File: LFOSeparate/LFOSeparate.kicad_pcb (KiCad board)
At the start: 2 copper layers, 100 x 45 mm, 31 parts, among them IC1 PIC16F15325-I_P, IC2 MCP6232-E_P, IC3 MCP6232-E_P, J1 ICSP, J2 D_Power, J3 Input, J4 Output, J5 A_Power, U1 Opamp_Dual

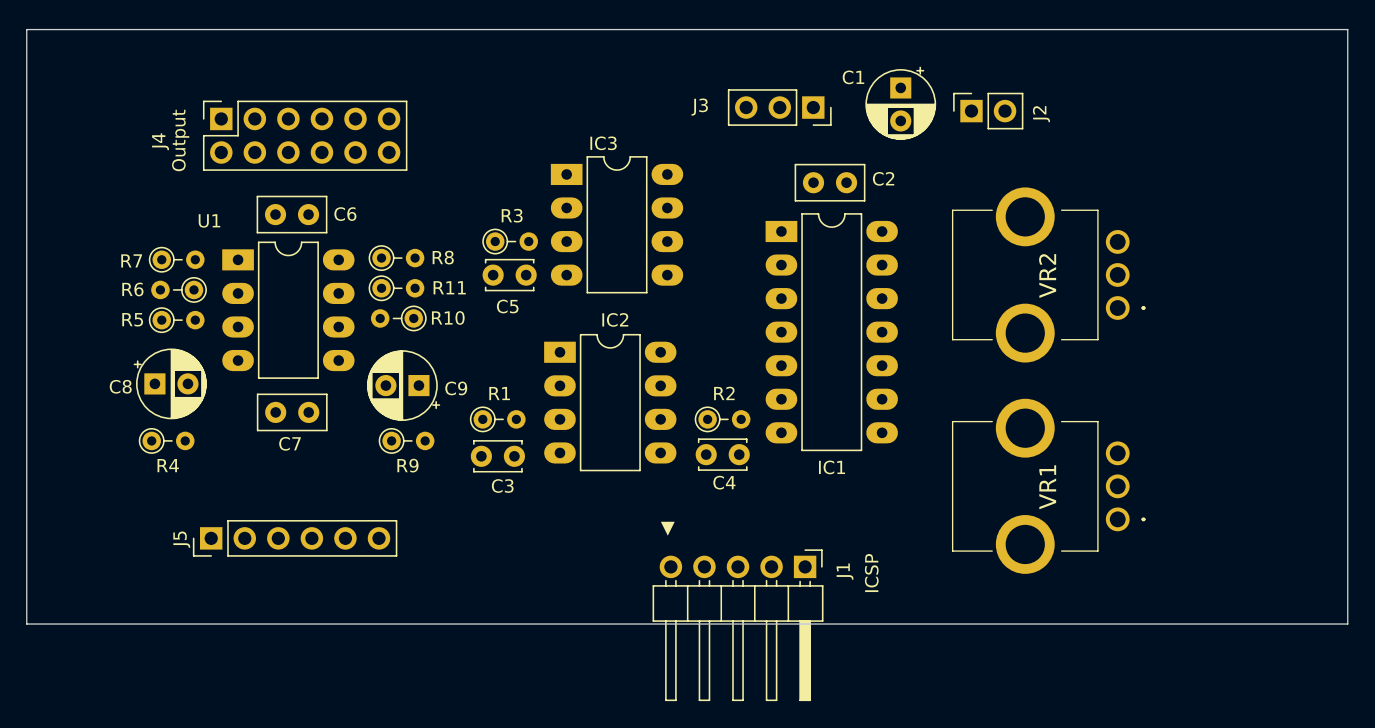
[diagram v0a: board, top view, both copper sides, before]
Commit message: LFOSeparate
LFOSeparateは配線完了
EGSeparateは回路図作成中
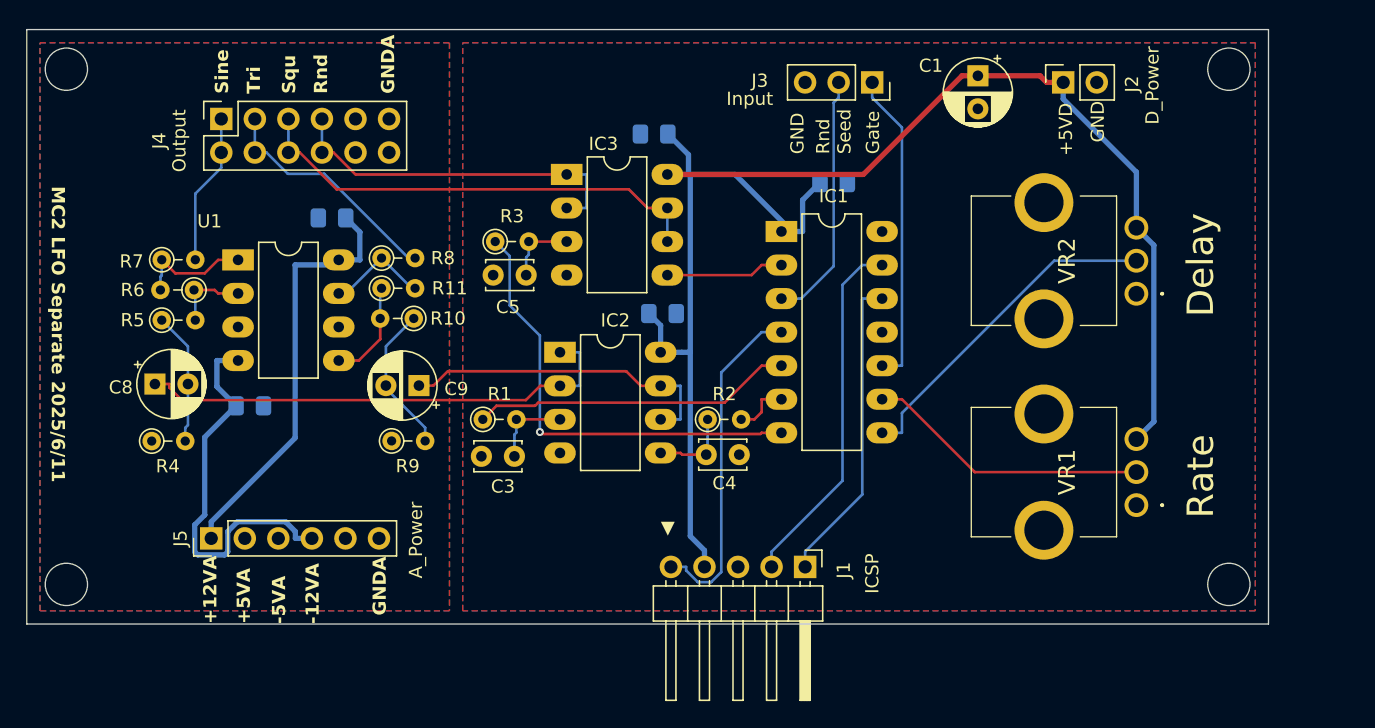
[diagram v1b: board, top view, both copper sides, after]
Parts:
- added C10: 0.1uF, Capacitor_SMD:C_0805_2012Metric_Pad1.18x1.45mm_HandSolder, B.Cu at (134.5, 41.9)
- added C11: 0.1uF, Capacitor_SMD:C_0805_2012Metric_Pad1.18x1.45mm_HandSolder, B.Cu at (135.1, 55.5)
- C2, C6, C7: footprint Capacitor_THT:C_Disc_D5.0mm_W2.5mm_P2.50mm -> Capacitor_SMD:C_0805_2012Metric_Pad1.18x1.45mm_HandSolder; moved to B.Cu
- moved J2 7.28 mm to (165.5, 38.0)
- moved C1 5.91 mm to (159.0, 37.5)
- moved J3 4.85 mm to (151.0, 38.0)
- moved C7 2.02 mm to (103.9, 62.5)
- moved C6 1.80 mm to (110.1, 48.3)
- moved VR1 1.78 mm to (171.0, 70.0)
- moved VR2 1.78 mm to (171.0, 54.0)
- moved C2 1.52 mm to (148.1, 45.6)
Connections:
- VR1 pad 1: +5VD -> GND
- VR1 pad 3: GND -> +5VD
- VR2 pad 1: +5VD -> GND
- VR2 pad 3: GND -> +5VD
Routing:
- net +5VD: track 0.00 -> 120.1 mm
- net Raw_Sine: track 0.00 -> 37.3 mm
- net Square: track 0.00 -> 35.5 mm
- net PWM_Randum: track 0.00 -> 34.2 mm, vias 0 -> 1
- net +12VA: track 0.00 -> 32.0 mm
- net -12VA: track 0.00 -> 29.7 mm
- net Randum: track 0.00 -> 27.3 mm
- net ICSPDT: track 0.00 -> 27.2 mm
- net ~MCLR: track 0.00 -> 25.7 mm
- net Delay: track 0.00 -> 25.5 mm
- net Raw_Triangle: track 0.00 -> 24.7 mm
- net PWM_Sine: track 0.00 -> 24.3 mm
- net Gate: track 0.00 -> 23.9 mm
- net ICSPCLK: track 0.00 -> 23.6 mm
- net Rate: track 0.00 -> 21.5 mm
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- added copper zone on B.Cu, net GND
- added copper zone on F.Cu, net GND
- added copper zone on B.Cu, net GNDA
- added copper zone on F.Cu, net GNDA
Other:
- board size 100 x 45 mm -> 94 x 45 mm
- board text added: "+12VA"
- board text added: "+5VA"
- board text added: "+5VD"
- board text added: "-12VA"
- board text added: "-5VA"
- board text added: "A_Power"
- board text added: "D_Power"
- board text added: "Delay"
- board text added: "GND"
- board text added: "GNDA"
- board text added: "Gate"
- board text added: "Input"
- board text added: "MC2 LFO Separate 2025/6/11"
- board text added: "Rate"
- board text added: "Rnd"
- board text added: "Rnd Seed"
- board text added: "Sine"
- board text added: "Squ"
- board text added: "Tri"

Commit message: MC2
アクセントレベルを追加したEGACCを登録
回路全般部品配置済
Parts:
- added D1: D, Diode_THT:D_DO-34_SOD68_P2.54mm_Vertical_AnodeUp, F.Cu at (94.1, 37.7)
- added D2: LED, LED_THT:LED_D5.0mm_FlatTop, F.Cu at (89.4, 56.6)
- added Q1: Q_NPN_ECB, Package_TO_SOT_THT:TO-92_HandSolder, F.Cu at (91.8, 45.2)
- added R12: 100K, Resistor_THT:R_Axial_DIN0204_L3.6mm_D1.6mm_P2.54mm_Vertical, F.Cu at (94.3, 40.3)
- added R13: 1K, Resistor_THT:R_Axial_DIN0204_L3.6mm_D1.6mm_P2.54mm_Vertical, F.Cu at (92.2, 49.1)
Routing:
- net +12VA: track 32.0 -> 52.3 mm
- net Net-(D2-A): track 0.00 -> 12.0 mm
- net Triangle: track 18.8 -> 27.7 mm
- net Net-(Q1-B): track 0.00 -> 5.97 mm
- net Net-(Q1-C): track 0.00 -> 5.58 mm
- net Net-(D1-K): track 0.00 -> 2.61 mm
- net -12VA: track 29.7 -> 32.1 mm
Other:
- board text added: "MC2 LFO Separate 2025/6/14"
- board text removed: "MC2 LFO Separate 2025/6/11"

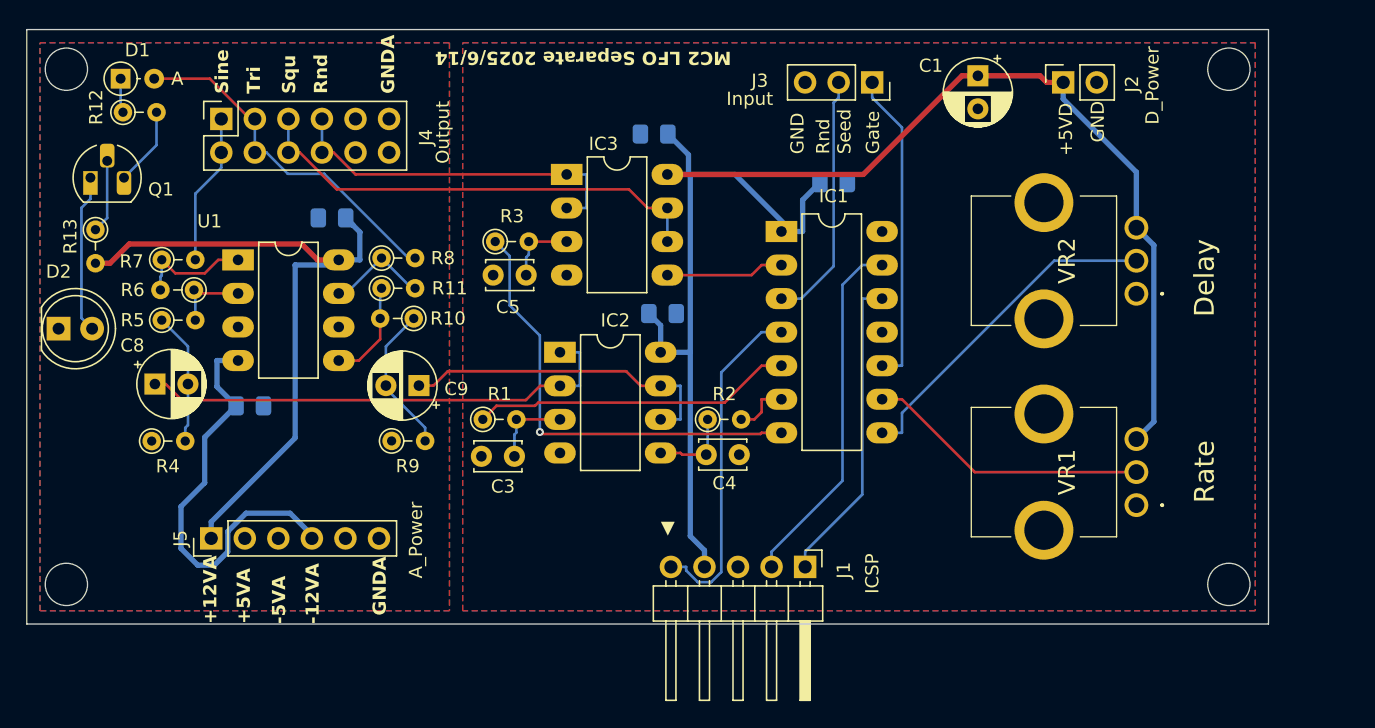
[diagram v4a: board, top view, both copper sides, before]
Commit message: LFOSeparate
プログラムと回路のデバッグ後の修正を反映
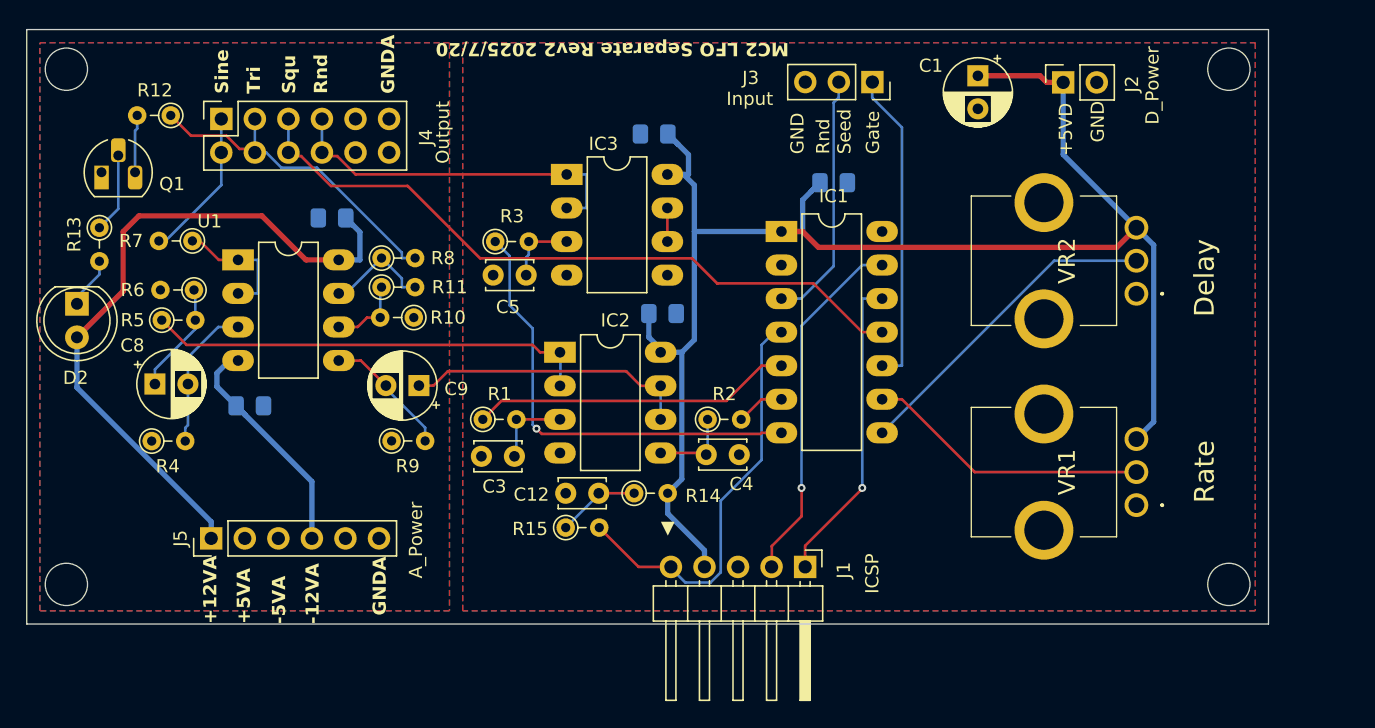
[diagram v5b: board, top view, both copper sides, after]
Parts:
- removed D1: D, Diode_THT:D_DO-34_SOD68_P2.54mm_Vertical_AnodeUp
- added C12: 0.01uF, Capacitor_THT:C_Disc_D3.4mm_W2.1mm_P2.50mm, F.Cu at (130.3, 69.1)
- added R14: 1K, Resistor_THT:R_Axial_DIN0204_L3.6mm_D1.6mm_P2.54mm_Vertical, F.Cu at (133.0, 69.1)
- added R15: 100, Resistor_THT:R_Axial_DIN0204_L3.6mm_D1.6mm_P2.54mm_Vertical, F.Cu at (127.8, 71.7)
- C8, C9: value 1uF/16V -> 47uF/16V
- R11: value 12K -> 1.2K
- R13: value 1K -> 2.2K
- R5: value 10K -> 30K
- R6: value 3.9K -> 20K
- moved R12 3.62 mm to (97.9, 40.5), turned to 180 degrees
- moved R7 2.72 mm to (99.5, 50.0), turned to 180 degrees
- moved D2 2.34 mm to (90.8, 54.8), turned to -90 degrees
- moved Q1 0.93 mm to (92.7, 44.8)
- moved R13 0.33 mm to (92.5, 49.0)
- moved R11 0.08 mm to (113.9, 53.5)
- moved R10 0.07 mm to (116.3, 55.8)
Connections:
- C8 pad 1: Raw_Sine -> Net-(C8-Pad1)
- C8 pad 2: Net-(C8-Pad2) -> Net-(U1A-+)
- C9 pad 2: Net-(C9-Pad2) -> Net-(U1B-+)
- D2 pad 1: GNDA -> Net-(D2-K)
- D2 pad 2: Net-(D2-A) -> +12VA
- IC1 pad 11: unconnected-(IC1-RA2-Pad11) -> Square
- IC1 pad 2: Raw_Square -> unconnected-(IC1-RA5-Pad2)
- IC3 pad 5: Raw_Square -> GND
- IC3 pad 6: Square -> Net-(IC3-VINB-)
- IC3 pad 7: Square -> Net-(IC3-VINB-)
- Q1 pad 1: Net-(D2-A) -> GNDA
- R10 pad 1: Net-(C9-Pad2) -> GNDA
- R10 pad 2: Net-(U1B-+) -> Net-(U1B--)
- R11 pad 1: Net-(U1B-+) -> Net-(U1B--)
- R12 pad 1: Net-(D1-K) -> Triangle
- R13 pad 2: +12VA -> Net-(D2-K)
- R4 pad 2: Net-(C8-Pad2) -> Net-(U1A-+)
- R5 pad 1: Net-(C8-Pad2) -> Raw_Sine
- R5 pad 2: Net-(U1A--) -> Net-(C8-Pad1)
- R6 pad 1: Net-(U1A--) -> Net-(C8-Pad1)
- R6 pad 2: Net-(R6-Pad2) -> GNDA
- R7 pad 1: Net-(R6-Pad2) -> Net-(U1A--)
- R9 pad 2: Net-(C9-Pad2) -> Net-(U1B-+)
- U1 pad 1: Net-(R6-Pad2) -> Net-(U1A--)
- U1 pad 3: GNDA -> Net-(U1A-+)
- U1 pad 6: GNDA -> Net-(U1B--)
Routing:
- net Square: track 35.5 -> 53.1 mm
- net -12VA: track 32.1 -> 18.5 mm
- net Net-(D2-A): track 12.0 -> 0.00 mm
- net Net-(C9-Pad2): track 11.4 -> 0.00 mm
- net Net-(U1A-+): track 0.00 -> 11.2 mm
- net Net-(C8-Pad2): track 10.1 -> 0.00 mm
- net Net-(R6-Pad2): track 8.95 -> 0.00 mm
- net Raw_Square: track 8.95 -> 0.00 mm
- net Net-(C8-Pad1): track 0.00 -> 8.43 mm
- net Net-(C12-Pad1): track 0.00 -> 6.32 mm
- net ~MCLR: track 25.7 -> 31.7 mm
- net Net-(U1B--): track 0.00 -> 5.78 mm
- net Net-(D2-K): track 0.00 -> 3.92 mm
- net Net-(U1A--): track 5.77 -> 9.60 mm
- net Raw_Sine: track 37.2 -> 33.8 mm
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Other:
- board text added: "MC2 LFO Separate Rev2 2025/7/20"
- board text removed: "MC2 LFO Separate 2025/6/14"

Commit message: MC2
ここまででFIXした内容
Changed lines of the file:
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@@
 			(drillshape 0)
 			(scaleselection 1)
-			(outputdirectory "gabar-data/")
+			(outputdirectory "gabar-data_Rev2/")
 		)
 	)
@@
 		)
 		(fp_text user "${REFERENCE}"
-			(at 2.77 5.08 0)
+			(at 2.032 -3.429 0)
 			(layer "F.Fab")
 			(effects
@@
 	)
 	(segment
-		(start 107.0755 43.5755)
-		(end 107.767218 43.5755)
+		(start 107.0755 43.9565)
+		(end 108.9587 45.8397)
 		(width 0.2)
 		(layer "F.Cu")
@@
 	)
 	(segment
-		(start 110.031418 45.8397)
+		(start 108.9587 45.8397)
 		(end 115.842 45.8397)
 		(width 0.2)
@@
 	)
 	(segment
-		(start 139.267 53.2178)
-		(end 146.56 53.2178)
+		(start 106.807 43.307)
+		(end 107.0755 43.5755)
 		(width 0.2)
 		(layer "F.Cu")
@@
 	)
 	(segment
-		(start 107.767218 43.5755)
-		(end 110.031418 45.8397)
+		(start 139.267 53.2178)
+		(end 146.56 53.2178)
 		(width 0.2)
 		(layer "F.Cu")
@@
 	)
 	(segment
-		(start 146.56 53.2178)
-		(end 150.248 56.906)
+		(start 115.842 45.8397)
+		(end 121.32 51.318)
 		(width 0.2)
 		(layer "F.Cu")
@@
 	)
 	(segment
-		(start 121.32 51.318)
-		(end 137.367 51.318)
+		(start 146.56 53.2178)
+		(end 150.248 56.906)
 		(width 0.2)
 		(layer "F.Cu")
@@
 	)
 	(segment
-		(start 150.248 56.906)
-		(end 151.75 56.906)
+		(start 121.32 51.318)
+		(end 137.367 51.318)
 		(width 0.2)
 		(layer "F.Cu")
@@
 	)
 	(segment
-		(start 106.807 43.307)
-		(end 107.0755 43.5755)
+		(start 107.0755 43.5755)
+		(end 107.0755 43.9565)
 		(width 0.2)
 		(layer "F.Cu")
@@
 	)
 	(segment
-		(start 115.842 45.8397)
-		(end 121.32 51.318)
+		(start 150.248 56.906)
+		(end 151.75 56.906)
 		(width 0.2)
 		(layer "F.Cu")
@@
 	)
 	(segment
-		(start 109.6155 43.5755)
-		(end 110.499 43.5755)
+		(start 109.6155 43.7025)
+		(end 110.881 44.968)
 		(width 0.2)
 		(layer "F.Cu")
@@
 	)
 	(segment
-		(start 111.891 44.968)
+		(start 110.881 44.968)
 		(end 127.874 44.968)
 		(width 0.2)
@@
 	)
 	(segment
-		(start 110.499 43.5755)
-		(end 111.891 44.968)
+		(start 109.6155 43.5755)
+		(end 109.6155 43.7025)
 		(width 0.2)
 		(layer "F.Cu")
@@
 	)
 	(segment
-		(start 116.397 51.298)
-		(end 115.395 51.298)
+		(start 115.395 50.8829)
+		(end 108.971 44.4587)
 		(width 0.2)
 		(layer "B.Cu")
@@
 	)
 	(segment
-		(start 105.1303 43.307)
-		(end 104.267 43.307)
+		(start 105.1647 44.4587)
+		(end 104.267 43.561)
 		(width 0.2)
 		(layer "B.Cu")
@@
 	)
 	(segment
-		(start 106.282 44.4587)
-		(end 105.1303 43.307)
+		(start 108.971 44.4587)
+		(end 105.1647 44.4587)
 		(width 0.2)
 		(layer "B.Cu")
@@
 	)
 	(segment
-		(start 108.971 44.4587)
-		(end 106.282 44.4587)
+		(start 116.397 51.298)
+		(end 115.395 51.298)
 		(width 0.2)
 		(layer "B.Cu")
@@
 	)
 	(segment
-		(start 115.395 50.8829)
-		(end 108.971 44.4587)
+		(start 115.395 51.298)
+		(end 115.395 50.8829)
 		(width 0.2)
 		(layer "B.Cu")
@@
 	)
 	(segment
-		(start 104.267 40.767)
+		(start 104.267 43.561)
 		(end 104.267 43.307)
 		(width 0.2)
@@
 	)
 	(segment
-		(start 115.395 51.298)
-		(end 115.395 50.8829)
+		(start 104.267 40.767)
+		(end 104.267 43.307)
 		(width 0.2)
 		(layer "B.Cu")
